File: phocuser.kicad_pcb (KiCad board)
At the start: 2 copper layers, 35 x 40 mm, 52 parts, among them J1 Conn_01x04_Male, J2 Conn_ARM_JTAG_SWD_10, J3 Conn_01x02_Male, J4 DX07S016JA1R1500, J5 Accessory 0, J6 Accessory 1, J7 Accessory 2, U1 HolyIot-18010, U2 TMC2130-LA, U3 FT231XQ

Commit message: checkin
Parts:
- C11, C12, C13, C14, FB1, R6, R7, R8, R9, U3: moved to B.Cu
- moved J3 4.02 mm to (196.0, 98.0)
- moved C12 1.27 mm to (168.5, 94.8), turned to 270 degrees
- moved C13 1.27 mm to (171.5, 94.8), turned to 90 degrees
- moved R8 1.27 mm to (170.5, 94.8), turned to 90 degrees
- moved R9 1.27 mm to (169.5, 94.8), turned to 90 degrees
- moved J1 1.22 mm to (182.8, 101.0)
- turned C14 to 90 degrees
- turned R6 to 270 degrees

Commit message: Layout incremental checkin
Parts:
- removed C16, C17, C18: 100nf, Capacitor_SMD:C_0402_1005Metric
- removed J7: Accessory 2, Connector_JST:JST_PH_B4B-PH-K_1x04_P2.00mm_Vertical
- removed R15, R16: 47k, Resistor_SMD:R_0402_1005Metric
- removed TH2, TH3, TH4: Thermistor_NTC, Resistor_SMD:R_0402_1005Metric
- added D1: LED, LED_SMD:LED_0603_1608Metric, F.Cu at (181.0, 100.0)
- C11, C12, C13, C14, FB1, R6, R7, R8, R9: moved to F.Cu
- R14: value 47k -> 470
- U2: footprint Package_DFN_QFN:QFN-36-1EP_5x6mm_P0.5mm_EP3.6x4.1mm -> Package_DFN_QFN:QFN-36-1EP_5x6mm_P0.5mm_EP3.6x4.1mm_ThermalVias
- U3: footprint Package_DFN_QFN:QFN-20-1EP_4x4mm_P0.5mm_EP2.5x2.5mm -> Package_DFN_QFN:QFN-20-1EP_4x4mm_P0.5mm_EP2.5x2.5mm_ThermalVias; moved to F.Cu
- moved C9 65.6 mm to (194.9, 91.9), turned to 270 degrees
- moved C6 60.8 mm to (193.8, 91.9), turned to 270 degrees
- moved C7 58.5 mm to (195.1, 84.6), turned to 180 degrees
- moved R12 57.6 mm to (187.3, 85.5), turned to 90 degrees
- moved R1 56.3 mm to (190.5, 95.0), turned to 90 degrees
- moved TH1 55.9 mm to (182.2, 70.8), turned to 180 degrees
- moved R13 46.3 mm to (182.2, 71.8), turned to 180 degrees
- moved R14 45.2 mm to (181.0, 97.2), turned to 90 degrees
- moved C15 44.8 mm to (182.2, 72.8)
- moved J3 17.0 mm to (196.5, 81.0), turned to 180 degrees
- moved J5 12.7 mm to (187.5, 67.8)
- moved C5 12.4 mm to (181.5, 88.5), turned to 270 degrees
- moved C1 8.51 mm to (192.2, 95.2)
- moved C2 7.75 mm to (188.2, 95.0), turned to 180 degrees
- moved J6 6.66 mm to (190.8, 73.5)
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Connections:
- C2 pad 2: GNDA -> GND
- C4 pad 2: GNDS -> GND
- C5 pad 1: GNDS -> GND
- C7 pad 2: GNDS -> GND
- C8 pad 2: GNDS -> GND
- C9 pad 2: GNDS -> GND
- J3 pad 2: GNDS -> GND
- R14 pad 1: THERM1 -> Net-(D1-Pad2)
- R14 pad 2: VCC -> VBUS
- R2 pad 1: GNDS -> GND
- R3 pad 2: GNDS -> GND
- U1 pad 10: ACC0_A -> ACC1_A
- U1 pad 11: ACC0_B -> MISO
- U1 pad 12: Net-(U1-Pad12) -> STEP
- U1 pad 13: Net-(U1-Pad13) -> DIR
- U1 pad 15: RXD -> Net-(U1-Pad15)
- U1 pad 16: TXD -> Net-(U1-Pad16)
- U1 pad 2: ACC2_A -> TMCCLK
- U1 pad 26: MISO -> TXD
- U1 pad 27: MOSI -> RXD
- U1 pad 28: SCLK -> Net-(U1-Pad28)
- U1 pad 29: ~CS1 -> Net-(U1-Pad29)
- U1 pad 3: ACC2_B -> ~CS1
- U1 pad 30: TMCCLK -> Net-(U1-Pad30)
- U1 pad 33: DIR -> Net-(U1-Pad33)
- U1 pad 34: STEP -> Net-(U1-Pad34)
- U1 pad 4: ACC1_A -> SCLK
- U1 pad 5: ACC1_B -> MOSI
- U1 pad 6: THERM0 -> ACC0_A
- U1 pad 7: THERM1 -> ACC0_B
- U1 pad 8: THERM2 -> THERM0
- U1 pad 9: THERM3 -> ACC1_B
- U2 pad 12: GNDS -> GND
- U2 pad 24: GNDA -> GND
- U2 pad 35: GNDS -> GND
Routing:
- net GND: track 0.00 -> 47.7 mm, vias 0 -> 26
- net TMCCLK: track 0.00 -> 24.9 mm, vias 0 -> 1
- net ~MOTOR_EN: track 0.00 -> 24.4 mm, vias 0 -> 1
- net ~CS1: track 0.00 -> 23.3 mm, vias 0 -> 1
- net DIAG1: track 0.00 -> 23.1 mm, vias 0 -> 1
- net SCLK: track 0.00 -> 22.1 mm, vias 0 -> 1
- net DIAG0: track 0.00 -> 21.9 mm, vias 0 -> 1
- net MOSI: track 0.00 -> 20.4 mm, vias 0 -> 1
- net ~RESET: track 0.00 -> 18.8 mm, vias 0 -> 2
- net Net-(C11-Pad1): track 0.00 -> 18.3 mm, vias 0 -> 2
- net Net-(J1-Pad1): track 0.00 -> 15.5 mm, vias 0 -> 2
- net MISO: track 0.00 -> 14.5 mm, vias 0 -> 1
- net Net-(J1-Pad4): track 0.00 -> 14.4 mm, vias 0 -> 2
- net ACC1_B: track 0.00 -> 14.2 mm
- net Net-(J1-Pad2): track 0.00 -> 14.1 mm, vias 0 -> 2
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- added copper zone on In1.Cu, net +12V
- added copper zone on B.Cu, net GND
- added copper zone on In2.Cu, net GND
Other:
- copper layers 2 -> 4
- net class Default: clearance 0.2 -> 0.1524; trace_width 0.25 -> 0.1524; via_dia 0.8 -> 0.508; via_drill 0.4 -> 0.254
- rule trace_clearance: 0.2 -> 0.1524
- rule trace_min: 0.2 -> 0.127
- rule via_min_drill: 0.3 -> 0.254
- rule via_min_size: 0.4 -> 0.508

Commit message: layout complete
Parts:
- added C16: 100nf, Capacitor_SMD:C_0402_1005Metric, F.Cu at (173.9, 82.3)
- added C17: 100nf, Capacitor_SMD:C_0402_1005Metric, F.Cu at (178.3, 89.6)
- added C18: 100nf, Capacitor_SMD:C_0402_1005Metric, F.Cu at (178.0, 85.5)
- added J7: Accessory 1, Connector_JST:JST_PH_B4B-PH-K_1x04_P2.00mm_Vertical, F.Cu at (168.5, 84.7)
- added U4: TLV76033DBZT, footprints:TLV76033DBZT, F.Cu at (178.7, 87.5)
- moved R10 5.32 mm to (176.0, 80.3)
- moved R11 5.32 mm to (174.9, 80.3)
- moved J2 0.30 mm to (176.7, 71.0)
- moved J5 0.30 mm to (187.2, 67.8)
- moved J6 0.27 mm to (191.0, 73.6)
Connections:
- R17 pad 1: DP -> Net-(J7-Pad2)
- R18 pad 1: DM -> Net-(J7-Pad3)
- R19 pad 1: VBUS -> Net-(C16-Pad1)
- U1 pad 26: TXD -> RXD
- U1 pad 27: RXD -> TXD
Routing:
- net Net-(C16-Pad1): track 0.00 -> 13.0 mm
- net Net-(J7-Pad3): track 0.00 -> 10.3 mm
- net Net-(J7-Pad2): track 0.00 -> 8.55 mm
- net VCC: track 8.89 -> 16.0 mm, vias 2 -> 6
- net TXD: track 3.69 -> 9.53 mm
- net VBUS: track 10.7 -> 14.4 mm
- net GND: track 47.7 -> 51.3 mm, vias 26 -> 32
- net ACC1_B: track 14.2 -> 12.5 mm
- net ACC1_A: track 12.1 -> 10.9 mm
- net Net-(R10-Pad2): track 10.9 -> 9.73 mm
- net RXD: track 4.68 -> 5.82 mm
- net TMCCLK: track 24.9 -> 24.4 mm
- added copper zone on In1.Cu, net VCC

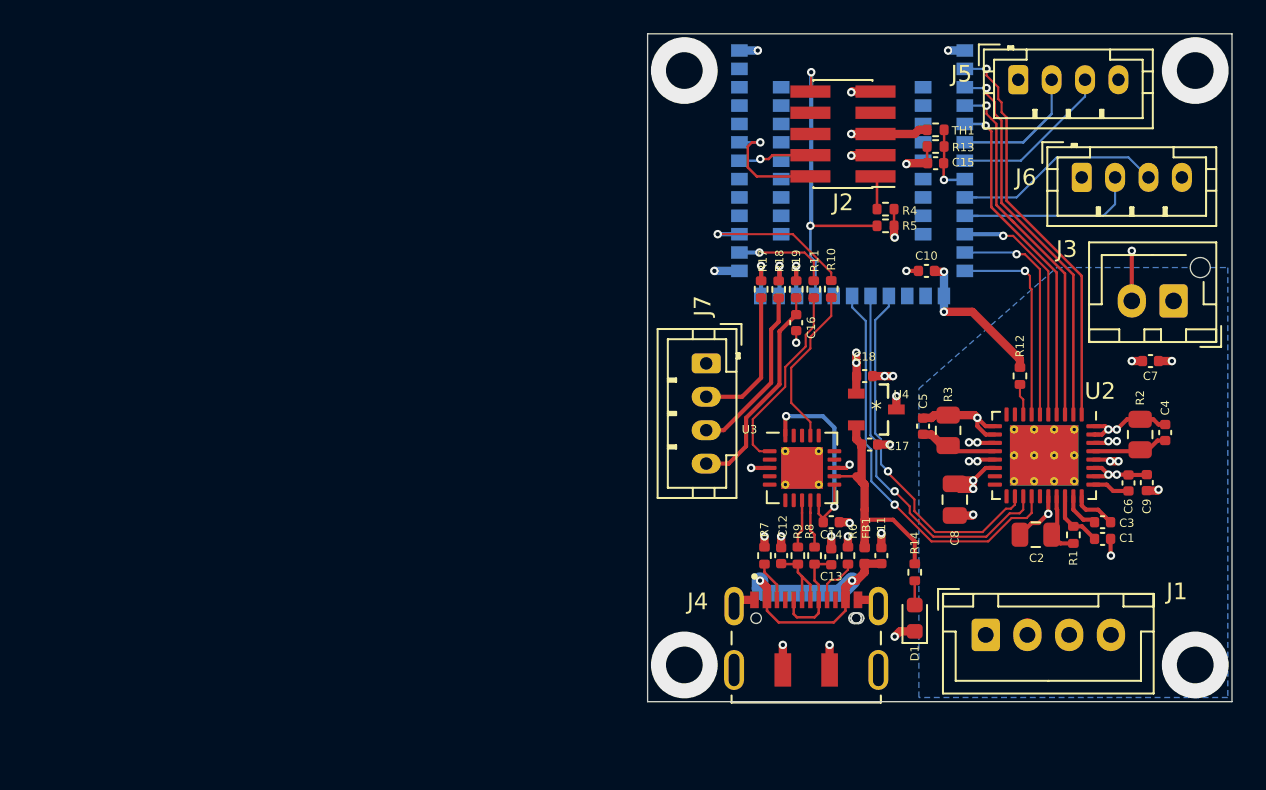
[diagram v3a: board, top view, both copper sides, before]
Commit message: cleanup and move to kicad 6.0
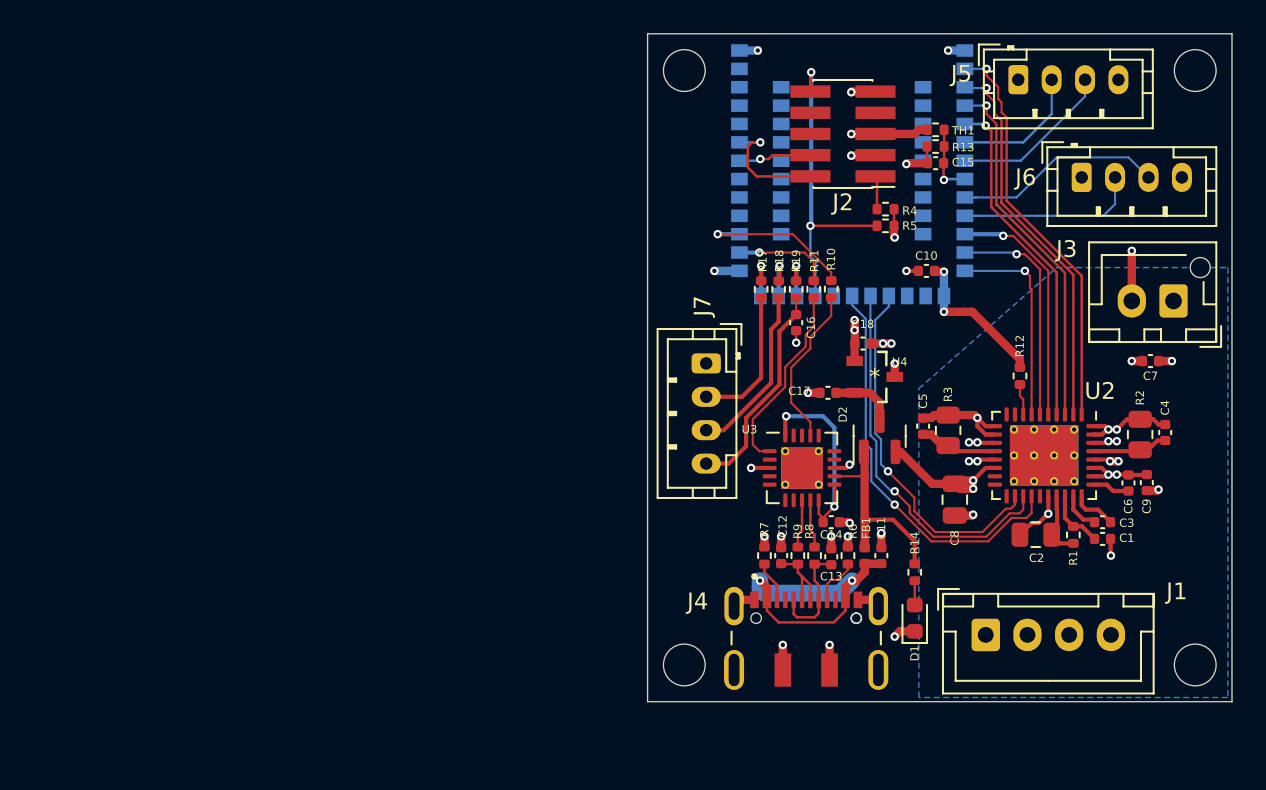
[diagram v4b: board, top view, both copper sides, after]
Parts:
- added D2: BAT54C, Package_TO_SOT_SMD:SOT-23, F.Cu at (178.9, 89.1)
- added H1: MountingHole, MountingHole:MountingHole_2.2mm_M2, F.Cu at (167.2, 67.2)
- added H2: MountingHole, MountingHole:MountingHole_2.2mm_M2, F.Cu at (197.8, 67.2)
- added H3: MountingHole, MountingHole:MountingHole_2.2mm_M2, F.Cu at (167.2, 102.8)
- added H4: MountingHole, MountingHole:MountingHole_2.2mm_M2, F.Cu at (197.8, 102.8)
- moved C17 3.98 mm to (175.8, 86.5), turned to 180 degrees
- moved C18 1.95 mm to (177.9, 83.6)
- moved U4 1.95 mm to (178.6, 85.6)
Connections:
- net ~CS1 renamed ~{CS1}
- net ~MOTOR_EN renamed ~{MOTOR_EN}
- net ~RESET renamed ~{RESET}
- C17 pad 1: VBUS -> Net-(C17-Pad1)
- J2 pad 6: Net-(J2-Pad6) -> unconnected-(J2-Pad6)
- J2 pad 7: Net-(J2-Pad7) -> unconnected-(J2-Pad7)
- J2 pad 8: Net-(J2-Pad8) -> unconnected-(J2-Pad8)
- J4 pad 10: Net-(J4-Pad10) -> unconnected-(J4-Pad10)
- J4 pad 4: Net-(J4-Pad4) -> unconnected-(J4-Pad4)
- U1 pad 15: Net-(U1-Pad15) -> unconnected-(U1-Pad15)
- U1 pad 16: Net-(U1-Pad16) -> unconnected-(U1-Pad16)
- U1 pad 20: Net-(U1-Pad20) -> unconnected-(U1-Pad20)
- U1 pad 28: Net-(U1-Pad28) -> unconnected-(U1-Pad28)
- U1 pad 29: Net-(U1-Pad29) -> unconnected-(U1-Pad29)
- U1 pad 30: Net-(U1-Pad30) -> unconnected-(U1-Pad30)
- U1 pad 33: Net-(U1-Pad33) -> unconnected-(U1-Pad33)
- U1 pad 34: Net-(U1-Pad34) -> unconnected-(U1-Pad34)
- U1 pad 35: Net-(U1-Pad35) -> unconnected-(U1-Pad35)
- U1 pad 36: Net-(U1-Pad36) -> unconnected-(U1-Pad36)
- U1 pad 38: Net-(U1-Pad38) -> unconnected-(U1-Pad38)
- U1 pad 39: Net-(U1-Pad39) -> unconnected-(U1-Pad39)
- U1 pad 40: Net-(U1-Pad40) -> unconnected-(U1-Pad40)
- U1 pad 41: Net-(U1-Pad41) -> unconnected-(U1-Pad41)
- U1 pad 42: Net-(U1-Pad42) -> unconnected-(U1-Pad42)
- U1 pad 43: Net-(U1-Pad43) -> unconnected-(U1-Pad43)
- U1 pad 44: Net-(U1-Pad44) -> unconnected-(U1-Pad44)
- U1 pad 45: Net-(U1-Pad45) -> unconnected-(U1-Pad45)
- U1 pad 46: Net-(U1-Pad46) -> unconnected-(U1-Pad46)
- U1 pad 47: Net-(U1-Pad47) -> unconnected-(U1-Pad47)
- U1 pad 48: Net-(U1-Pad48) -> unconnected-(U1-Pad48)
- U1 pad 49: Net-(U1-Pad49) -> unconnected-(U1-Pad49)
- U1 pad 50: Net-(U1-Pad50) -> unconnected-(U1-Pad50)
- U1 pad 51: Net-(U1-Pad51) -> unconnected-(U1-Pad51)
- U1 pad 52: Net-(U1-Pad52) -> unconnected-(U1-Pad52)
- U1 pad 53: Net-(U1-Pad53) -> unconnected-(U1-Pad53)
- U1 pad 54: Net-(U1-Pad54) -> unconnected-(U1-Pad54)
- U1 pad 55: Net-(U1-Pad55) -> unconnected-(U1-Pad55)
- U2 pad 10: Net-(U2-Pad10) -> unconnected-(U2-Pad10)
- U2 pad 17: Net-(U2-Pad17) -> unconnected-(U2-Pad17)
- U2 pad 18: Net-(U2-Pad18) -> unconnected-(U2-Pad18)
- U2 pad 19: Net-(U2-Pad19) -> unconnected-(U2-Pad19)
- U2 pad 23: Net-(U2-Pad23) -> unconnected-(U2-Pad23)
- U2 pad 9: Net-(U2-Pad9) -> unconnected-(U2-Pad9)
- U3 pad 14: Net-(U3-Pad14) -> unconnected-(U3-Pad14)
- U3 pad 15: Net-(U3-Pad15) -> unconnected-(U3-Pad15)
- U3 pad 16: Net-(U3-Pad16) -> unconnected-(U3-Pad16)
- U3 pad 18: Net-(U3-Pad18) -> unconnected-(U3-Pad18)
- U3 pad 19: Net-(U3-Pad19) -> unconnected-(U3-Pad19)
- U3 pad 2: Net-(U3-Pad2) -> unconnected-(U3-Pad2)
- U3 pad 4: Net-(U3-Pad4) -> unconnected-(U3-Pad4)
- U3 pad 5: Net-(U3-Pad5) -> unconnected-(U3-Pad5)
- U3 pad 6: Net-(U3-Pad6) -> unconnected-(U3-Pad6)
- U3 pad 7: Net-(U3-Pad7) -> unconnected-(U3-Pad7)
- U4 pad 2: VBUS -> Net-(C17-Pad1)
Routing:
- net +12V: track 9.64 -> 14.0 mm
- net Net-(C17-Pad1): track 0.00 -> 3.93 mm
- net VBUS: track 14.4 -> 12.4 mm
- net Net-(J1-Pad2): track 14.1 -> 13.6 mm
- net (no net): vias 4 -> 0
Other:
- net class Default removed
